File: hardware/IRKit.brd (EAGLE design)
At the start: 54 x 56 mm, 69 parts, among them CN1 USB-CONNECTORMICROB, IC1 ATMEGA32U4AU, IC2 TLV70233DBVT, IC3 LM386MM-1, IC4 GS1011MXXS, SW1 EVQPUJ02K, T1 2SD1781K, T2 BSS138

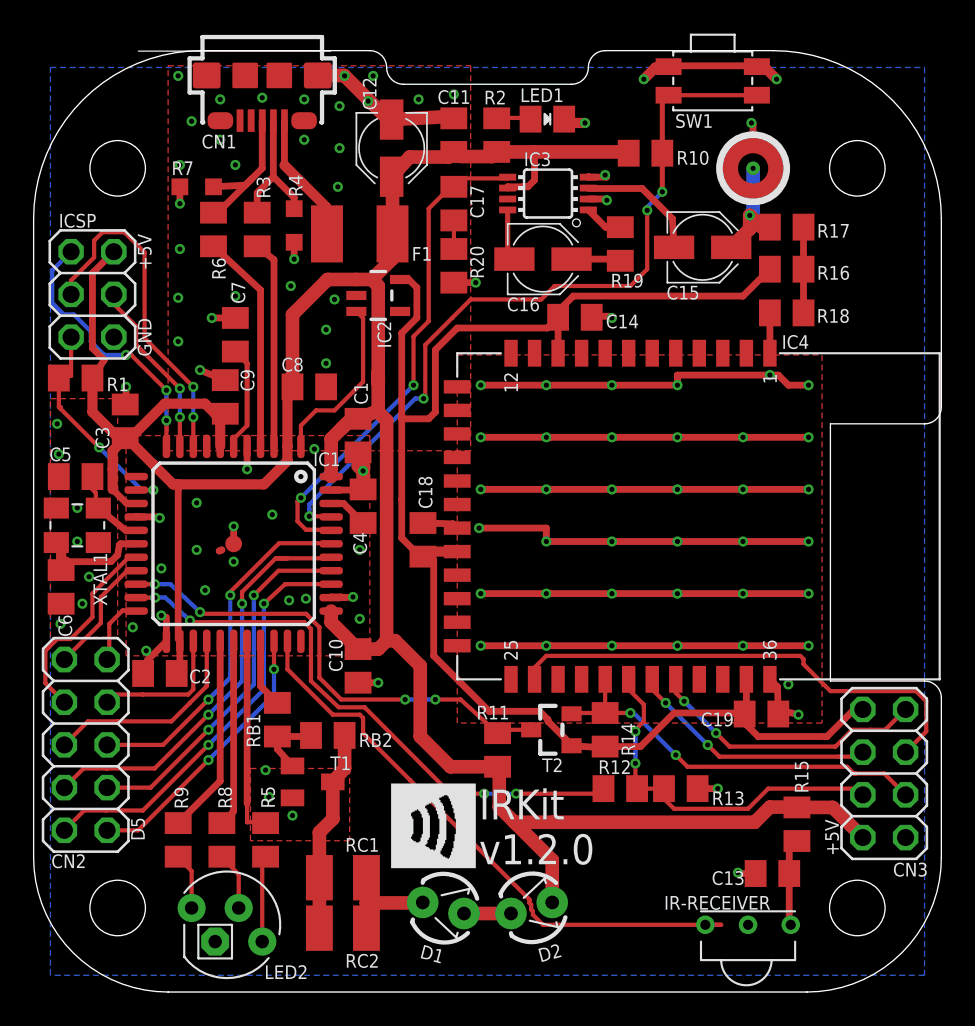
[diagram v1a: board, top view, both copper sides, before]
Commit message: changed C15 from electrolytic capacitor to ceramic capacitor
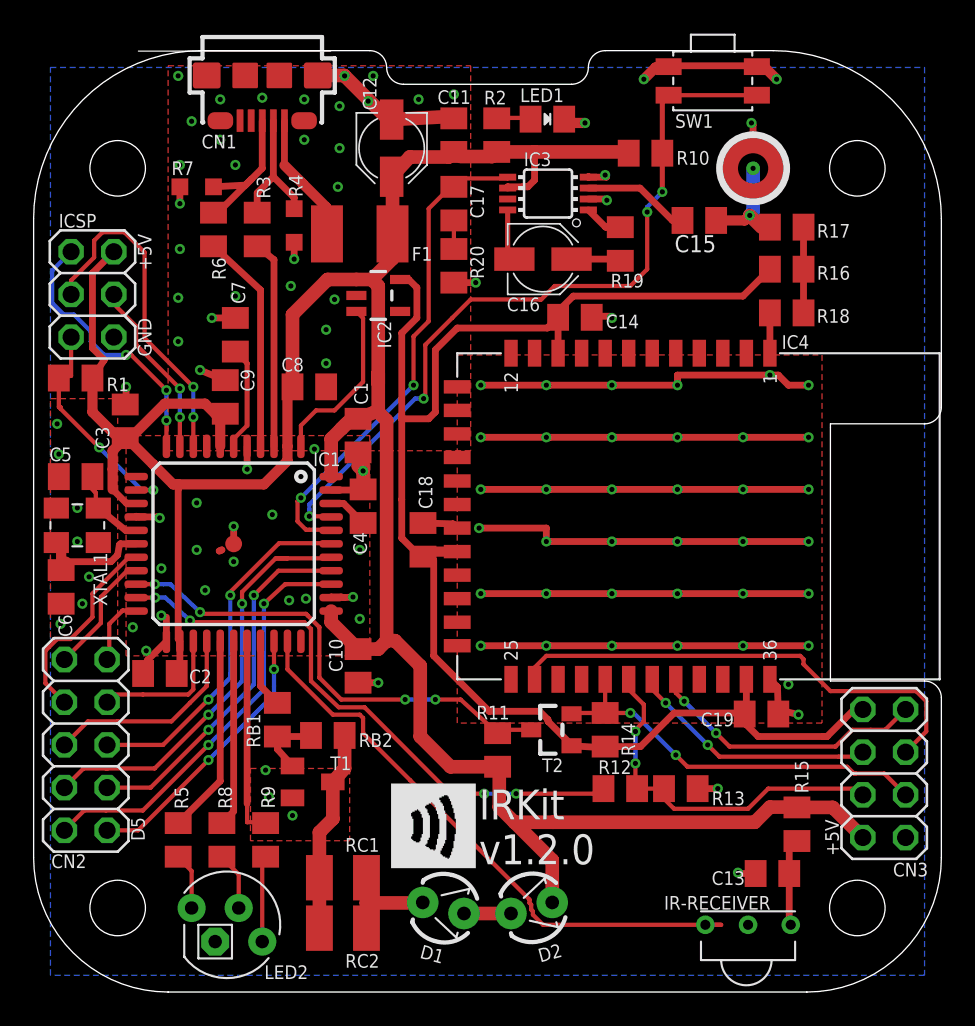
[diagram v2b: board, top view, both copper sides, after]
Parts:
- C15: device my:PANASONIC_B -> my:SMD2012
- C17: value 0.05uF -> 0.047uF
- R5: value 2.2k -> 1k
- R9: value 1k -> 2.2k
- moved R5 5.20 mm to (8.60, 9.05)
- moved R9 5.20 mm to (13.8, 9.05)
- moved C15 1.61 mm to (39.6, 45.9), turned to 180 degrees
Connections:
- net D6/LED_R: now also R5.1; no longer R9.1
- net D9/LED_G: now also R9.1; no longer R5.1
- net MICOUT: now also C15.1; no longer C15.+
- net N$4: now also C15.2; no longer C15.-
- net N$41: now also R5.2; no longer R9.2
- net N$5: now also R9.2; no longer R5.2
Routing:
- net N$4: track 7.46 -> 6.40 mm
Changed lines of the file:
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@@
 <attribute name="VALUE" x="25.314" y="15.162" size="0.8128" layer="27" rot="R270"/>
 </element>
-<element name="R9" library="my" package="SMD2012" value="1k" x="8.6" y="9.05" smashed="yes" rot="R270">
+<element name="R5" library="my" package="SMD2012" value="1k" x="8.6" y="9.05" smashed="yes" rot="R270">
 <attribute name="NAME" x="9.1965" y="10.888" size="0.8128" layer="25" rot="R90"/>
 <attribute name="VALUE" x="6.314" y="9.812" size="0.8128" layer="27" rot="R270"/>
@@
 </element>
 <element name="MIC" library="my" package="MIC_SMD_4MM" value="kus0223" x="42.8" y="49" smashed="yes"/>
-<element name="C15" library="my" package="PANASONIC_B" value="1uF" x="39.8" y="44.3" smashed="yes">
-<attribute name="NAME" x="37.65" y="41.2" size="0.8128" layer="25"/>
-<attribute name="VALUE" x="37.65" y="41.025" size="1.016" layer="27"/>
-</element>
 <element name="R17" library="my" package="SMD2012" value="2k" x="44.8" y="45.5" smashed="yes">
 <attribute name="NAME" x="46.6" y="44.875" size="0.8128" layer="25"/>
@@
 <attribute name="VALUE" x="36.8" y="43.5" size="1.016" layer="27" rot="R90"/>
 </element>
-<element name="C17" library="my" package="SMD2012" value="0.05uF" x="25" y="46.9" smashed="yes" rot="R270">
+<element name="C17" library="my" package="SMD2012" value="0.047uF" x="25" y="46.9" smashed="yes" rot="R270">
 <attribute name="NAME" x="25.975" y="48" size="0.8128" layer="25" rot="R270"/>
 <attribute name="VALUE" x="23.1" y="47.9" size="1.016" layer="27" rot="R270"/>
@@
 <attribute name="NAME" x="13.725" y="0.775" size="0.8128" layer="21"/>
 </element>
-<element name="R5" library="my" package="SMD2012" value="2.2k" x="13.8" y="9.05" smashed="yes" rot="R270">
+<element name="R9" library="my" package="SMD2012" value="2.2k" x="13.8" y="9.05" smashed="yes" rot="R270">
 <attribute name="NAME" x="14.35" y="10.925" size="0.8128" layer="25" rot="R90"/>
 <attribute name="VALUE" x="11.9" y="10.05" size="1.016" layer="27" rot="R270"/>
 </element>
+<element name="C15" library="my" package="SMD2012" value="1uF" x="39.6" y="45.9" rot="R180"/>
 </elements>
 <signals>
@@
 <contactref element="IC1" pad="29"/>
 <wire x1="12.7" y1="20.8625" x2="12.7" y2="11.2" width="0.4064" layer="1"/>
-<contactref element="R5" pad="1"/>
+<contactref element="R9" pad="1"/>
 <wire x1="12.7" y1="10.1" x2="13.8" y2="10.1" width="0.254" layer="1"/>
 <wire x1="12.7" y1="11" x2="12.7" y2="10.1" width="0.254" layer="1"/>
@@
 <signal name="D6/LED_R">
 <contactref element="IC1" pad="27"/>
-<contactref element="R9" pad="1"/>
+<contactref element="R5" pad="1"/>
 <wire x1="11.1" y1="20.8625" x2="11.1" y2="12.55" width="0.4064" layer="1"/>
 <wire x1="11.1" y1="12.55" x2="8.6" y2="10.05" width="0.4064" layer="1"/>
@@
 <wire x1="37.4" y1="49.9" x2="37.4" y2="47.6" width="0.3048" layer="1"/>
 <via x="37.4" y="47.6" extent="1-16" drill="0.3048"/>
-<via x="36.5" y="46.5" extent="1-16" drill="0.3048"/>
+<via x="36.5" y="46.4" extent="1-16" drill="0.3048"/>
 <wire x1="17.7" y1="28.2625" x2="17.6625" y2="28.3" width="0.254" layer="1"/>
 <wire x1="17.6625" y1="28.3" x2="16.4" y2="28.3" width="0.254" layer="1"/>
 <via x="16.4" y="28.3" extent="1-16" drill="0.3048"/>
 <wire x1="23.3" y1="38.5" x2="24.9" y2="40.1" width="0.254" layer="1"/>
-<wire x1="36.4" y1="46.5" x2="36.5" y2="46.5" width="0.254" layer="16"/>
+<wire x1="36.4" y1="46.5" x2="36.5" y2="46.4" width="0.254" layer="16"/>
 <wire x1="16.4" y1="28.3" x2="16.4" y2="28.7" width="0.254" layer="16"/>
 <via x="23.2" y="35.3" extent="1-16" drill="0.3048"/>
@@
 <wire x1="31" y1="42" x2="35.5" y2="42" width="0.254" layer="1"/>
 <wire x1="35.5" y1="42" x2="36.5" y2="43" width="0.254" layer="1"/>
-<wire x1="36.5" y1="43" x2="36.5" y2="46.5" width="0.254" layer="1"/>
-<wire x1="36.5" y1="46.5" x2="36.5" y2="46.7" width="0.254" layer="16"/>
+<wire x1="36.5" y1="43" x2="36.5" y2="46.4" width="0.254" layer="1"/>
+<wire x1="36.5" y1="46.4" x2="36.5" y2="46.7" width="0.254" layer="16"/>
 <wire x1="36.5" y1="46.7" x2="37.4" y2="47.6" width="0.254" layer="16"/>
 </signal>
@@
 <contactref element="MIC" pad="1"/>
 <contactref element="R17" pad="1"/>
-<contactref element="C15" pad="+"/>
 <wire x1="43.8" y1="45.5" x2="43.3" y2="45.5" width="0.4064" layer="1"/>
 <via x="42.6" y="46.2" extent="1-16" drill="0.3048"/>
-<wire x1="41.5" y1="44.3" x2="42.6" y2="45.4" width="0.8128" layer="1"/>
-<wire x1="42.6" y1="45.4" x2="42.6" y2="46.2" width="0.8128" layer="1"/>
 <wire x1="43.3" y1="45.5" x2="42.6" y2="46.2" width="0.8128" layer="1"/>
 <wire x1="42.6" y1="46.2" x2="42.8" y2="46.4" width="0.8128" layer="16"/>
 <wire x1="42.8" y1="46.4" x2="42.8" y2="49" width="0.8128" layer="16"/>
+<contactref element="C15" pad="1"/>
+<wire x1="40.6" y1="45.9" x2="42.3" y2="45.9" width="0.6096" layer="1"/>
+<wire x1="42.3" y1="45.9" x2="42.6" y2="46.2" width="0.6096" layer="1"/>
 </signal>
 <signal name="+2V">
@@
 <wire x1="45.8" y1="43" x2="45.8" y2="45.5" width="0.4064" layer="1"/>
 </signal>
-<signal name="N$4">
-<contactref element="C15" pad="-"/>
-<contactref element="IC3" pad="3"/>
-<wire x1="33.025" y1="47.8" x2="33" y2="47.825" width="0.3048" layer="1"/>
-<wire x1="38" y1="46" x2="38.1" y2="44.3" width="0.4064" layer="1"/>
-<wire x1="33.025" y1="47.8" x2="36.2" y2="47.8" width="0.4064" layer="1"/>
-<wire x1="36.2" y1="47.8" x2="38" y2="46" width="0.4064" layer="1"/>
-</signal>
 <signal name="N$6">
 <contactref element="IC3" pad="7"/>
@@
 <signal name="N$41">
 <contactref element="LED2" pad="4"/>
-<contactref element="R9" pad="2"/>
+<contactref element="R5" pad="2"/>
 <wire x1="9.4" y1="7.2" x2="8.6" y2="8" width="0.254" layer="1"/>
 <wire x1="9.4" y1="5" x2="9.4" y2="7.2" width="0.254" layer="1"/>
@@
 <signal name="N$5">
 <contactref element="LED2" pad="1"/>
-<contactref element="R5" pad="2"/>
+<contactref element="R9" pad="2"/>
 <wire x1="13.6" y1="7.8" x2="13.8" y2="8" width="0.254" layer="1"/>
 <wire x1="13.6" y1="3" x2="13.6" y2="7.8" width="0.254" layer="1"/>
 <wire x1="13.8" y1="8" x2="13.8" y2="8.05" width="0.254" layer="1"/>
 </signal>
+<signal name="N$4">
+<contactref element="C15" pad="2"/>
+<contactref element="IC3" pad="3"/>
+<wire x1="33" y1="47.825" x2="36.075" y2="47.825" width="0.4064" layer="1"/>
+<wire x1="36.075" y1="47.825" x2="38" y2="45.9" width="0.4064" layer="1"/>
+<wire x1="38" y1="45.9" x2="38.6" y2="45.9" width="0.4064" layer="1"/>
+</signal>
 </signals>

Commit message: added bypass capacitor near IR LEDs added varistor for Vusb
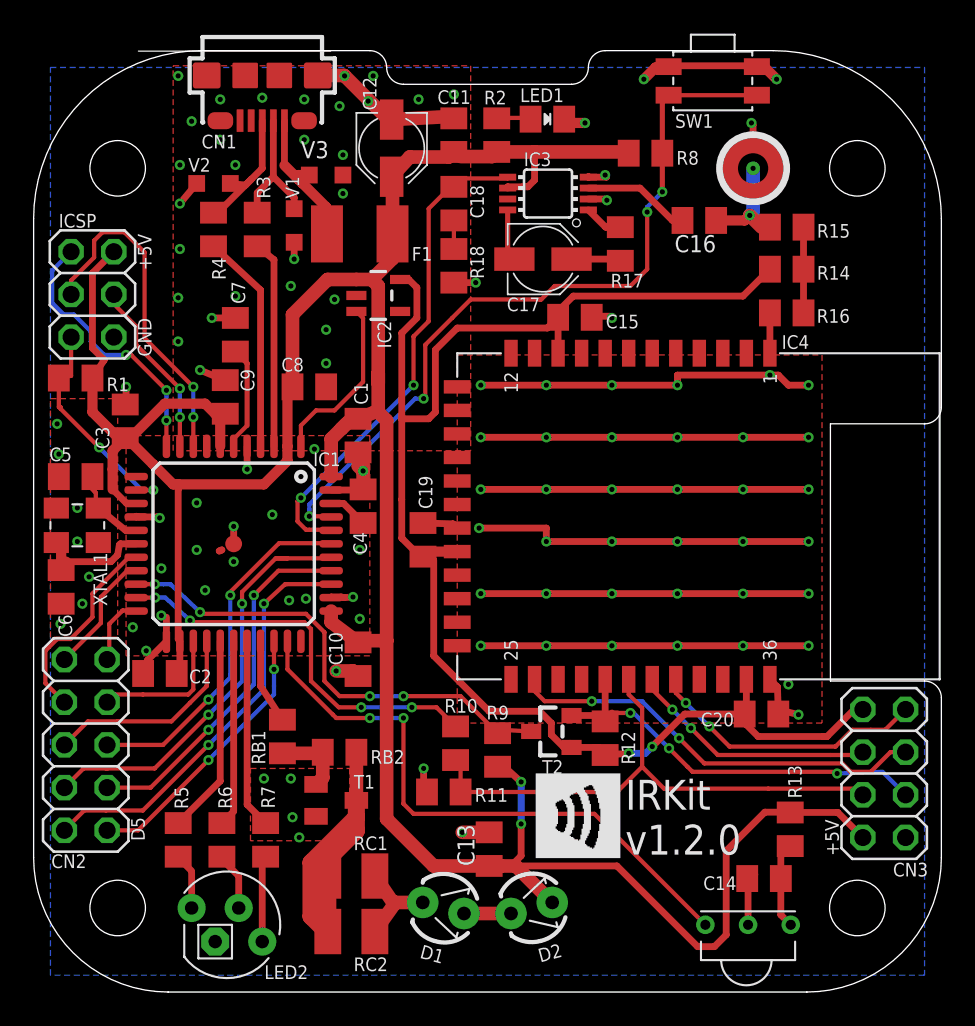
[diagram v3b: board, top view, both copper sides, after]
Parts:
- removed R19: 0, my:SMD2012
- removed R20: 10, my:SMD2012
- added C20: 0.1uF, my:SMD2012
- added V1, V2, V3: CG0603MLC-05E, my:CT/CN0603
- C13: value 4.7uF -> 1uF
- C14: value 0.1uF -> 4.7uF
- C15: value 1uF -> 0.1uF
- C16: value 10uF -> 1uF; device my:PANASONIC_B -> my:SMD2012
- C17: value 0.047uF -> 10uF; device my:SMD2012 -> my:PANASONIC_B
- C18: value 0.1uF -> 0.047uF
- R10: value 1k -> 2.2k
- R11: value 10k -> 3.3k
- R12: value 2.2k -> 4.7k
- R13: value 3.3k -> 220
- R14: value 4.7k -> 1.3k
- R15: value 220 -> 2k
- R16: value 1.3k -> 2k
- R17: value 2k -> 0
- R18: value 2k -> 10
- R4: value CG0603MLC-05E -> 22; device my:CT/CN0603 -> my:SMD2012
- R6: value 22 -> 1k
- R7: value CG0603MLC-05E -> 2.2k; device my:CT/CN0603 -> my:SMD2012
- R9: value 2.2k -> 10k
- moved R8 48.0 mm to (36.4, 49.9), turned to 0 degrees
- moved R7 39.1 mm to (13.8, 9.05), turned to 270 degrees
- moved R10 36.9 mm to (25.1, 14.8), turned to 90 degrees
- moved R6 36.3 mm to (11.2, 9.05), turned to 270 degrees
- moved R15 35.5 mm to (44.8, 45.5), turned to 0 degrees
- moved C14 35.2 mm to (43.5, 6.75)
- moved R14 29.5 mm to (44.8, 43.0), turned to 180 degrees
- moved C19 22.6 mm to (23.2, 26.9), turned to 270 degrees
- moved C18 20.1 mm to (25.0, 46.9)
- moved R18 20.0 mm to (25.0, 43.2), turned to 270 degrees
- moved C13 16.9 mm to (27.1, 8.50), turned to 90 degrees
- moved R9 14.8 mm to (27.6, 14.4)
- moved R17 9.95 mm to (34.9, 44.5), turned to 90 degrees
- moved C16 9.58 mm to (39.6, 45.9), turned to 180 degrees
- moved C15 9.38 mm to (32.2, 40.1)
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- renumbered U$2 to $1_61_$
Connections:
- net +2V: now also R14.1, R15.2, R16.2; no longer R16.1, R17.2, R18.2
- net +3V3: now also C15.2, C20.2, R12.2; no longer C14.2, C18.2, R16.2
- net +5V: now also C13.1, R13.2, R8.1, R9.2; no longer R10.1, R11.2, R15.2
- net A4/MIC: now also C18.1; no longer C17.1
- net A5/!RESET_SWITCH: now also R8.2; no longer R10.2
- net D0/WIFIRX: now also R9.1; no longer R11.1
- net D1/WIFITX: now also R10.2; no longer R12.2
- net D8/LED_B: now also R6.1; no longer R8.1
- net D9/LED_G: now also R7.1; no longer R9.1
- net GND: now also C14.2, C15.1, C20.1, R11.1, R16.1, R18.2, V1.2, V2.2, V3.2; no longer C14.1, C18.1, R13.1, R18.1, R20.2, R4.2, R7.2
- net MICOUT: now also C16.1, R15.1; no longer C15.1, R17.1
- net N$1: now also C17.-; no longer C16.-
- net N$14: now also C18.2, R18.1; no longer C17.2, R20.1
- net N$16: now also C14.1, R13.1; no longer C13.1, R15.1
- net N$17: now also R6.2; no longer R8.2
- net N$2: now also C17.+, R17.1; no longer C16.+, R19.1
- net N$4: now also C16.2; no longer C15.2
- net N$48: now also V1.1; no longer R4.1
- net N$5: now also R7.2; no longer R9.2
- net N$51: now also R4.2, V2.1; no longer R6.2, R7.1
- net N$52: now also V3.1
- net N$8: now also R17.2; no longer R19.2
- net USB+: now also R4.1; no longer R6.1
- net WIFI_UART0_RX: now also R10.1, R11.2; no longer R12.1, R13.2
- net WIFI_UART0_TX: now also R12.1; no longer R14.1
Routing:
- net +5V: track 168.4 -> 185.8 mm, vias 0 -> 2
- net WIFI_UART0_RX: track 22.2 -> 32.8 mm, vias 2 -> 0
- net D1/WIFITX: track 34.5 -> 24.0 mm
- net N$11: track 12.1 -> 21.6 mm
- net GND: track 179.7 -> 184.9 mm, vias 108 -> 109
- net WIFI_UART1_RTS: track 29.1 -> 25.2 mm, vias 0 -> 2
- net N$51: track 9.38 -> 8.38 mm
- net +3V3: track 92.3 -> 93.3 mm, vias 0 -> 2
- net D10/IROUT: track 4.08 -> 5.05 mm
- net WIFI_UART0_TX: track 23.9 -> 24.9 mm, vias 2 -> 3
- net N$52: track 8.66 -> 9.56 mm
- net D9/LED_G: track 11.9 -> 11.3 mm
- net IRLED: track 6.36 -> 5.80 mm
- net D13/IRIN: track 35.6 -> 35.8 mm, vias 0 -> 2

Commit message: close loop around IR LEDs move silk away from vias
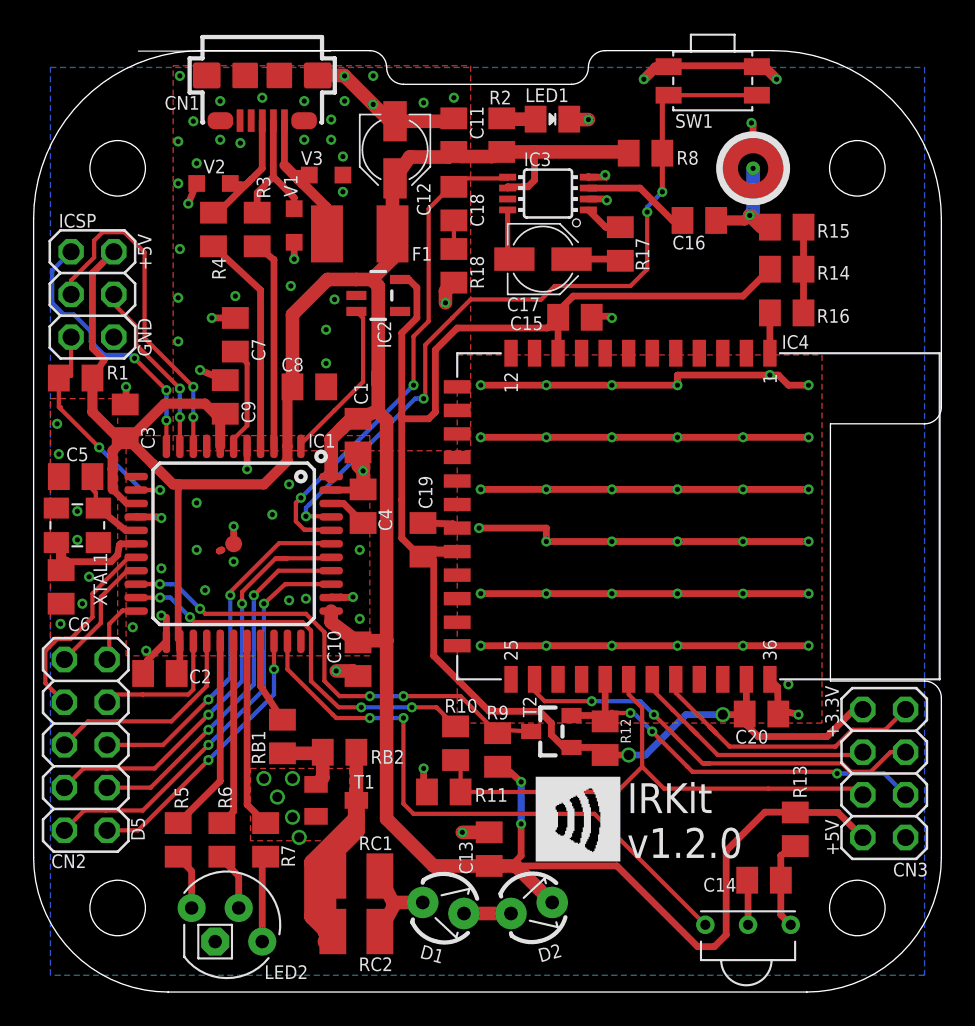
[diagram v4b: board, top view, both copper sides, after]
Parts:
- F1: value MF-MSMF050-2 -> MF-MSMF075-2
- moved R13 0.30 mm to (45.3, 9.68)
- moved LED1 0.30 mm to (30.9, 51.9)
- moved R2 0.30 mm to (27.9, 51.0)
- moved RC1 0.30 mm to (19.2, 6.90)
- moved RC2 0.30 mm to (19.2, 3.60)
- moved C12 0.22 mm to (21.5, 50.1)
- moved U$1 0.20 mm to (29.9, 7.80)
- moved C14 0.10 mm to (43.5, 6.65)
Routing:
- net !RESET: track 13.5 -> 14.3 mm
- net D7/LDO3.3_EN: track 10.4 -> 9.72 mm
- net WIFI_UART0_RTS: track 16.7 -> 17.3 mm, vias 2 -> 0
- net WIFI_UART0_CTS: track 14.8 -> 15.3 mm, vias 2 -> 0
- net GND: track 184.9 -> 184.5 mm, vias 109 -> 114
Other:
- board text added: "+3.3V"

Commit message: make 2012 pad smaller
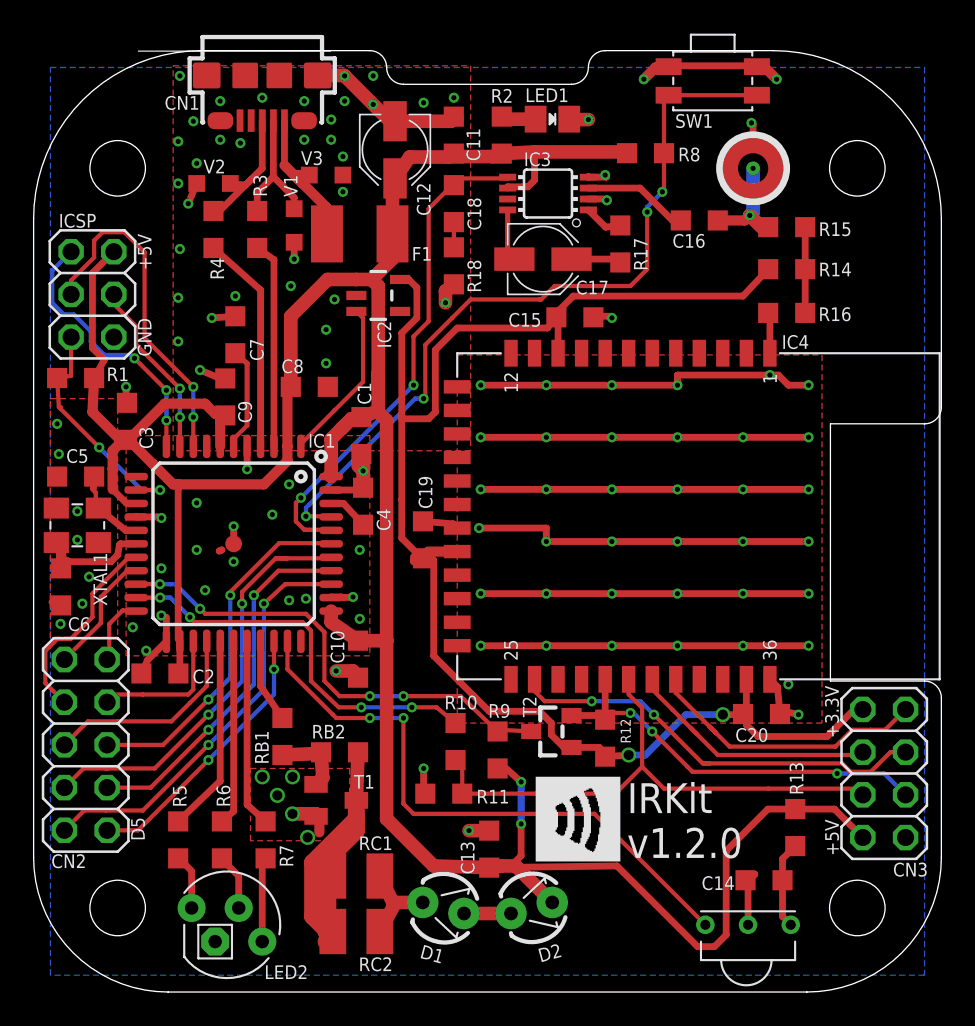
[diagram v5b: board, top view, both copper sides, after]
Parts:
- moved C1 0.20 mm to (19.5, 33.1)
- moved C3 0.10 mm to (5.55, 34.0)
- moved R10 0.10 mm to (25.1, 14.9)
- moved R11 0.10 mm to (24.4, 11.8)
- moved R13 0.10 mm to (45.3, 9.78)
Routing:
- net GND: track 184.5 -> 187.2 mm
- net A5/!RESET_SWITCH: track 46.3 -> 46.8 mm
